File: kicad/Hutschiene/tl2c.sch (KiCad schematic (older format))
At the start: 29 parts, among them IC101 ATTINY20-X, P101 12VDC, P102 RJ45, P103 CTL CONN, P104 TPI Header, P105 DRV CONN, P106 240VAC, P108 UG, P109 5VDC, P110 EG, P111 OG, SW101 TL3315NF160Q

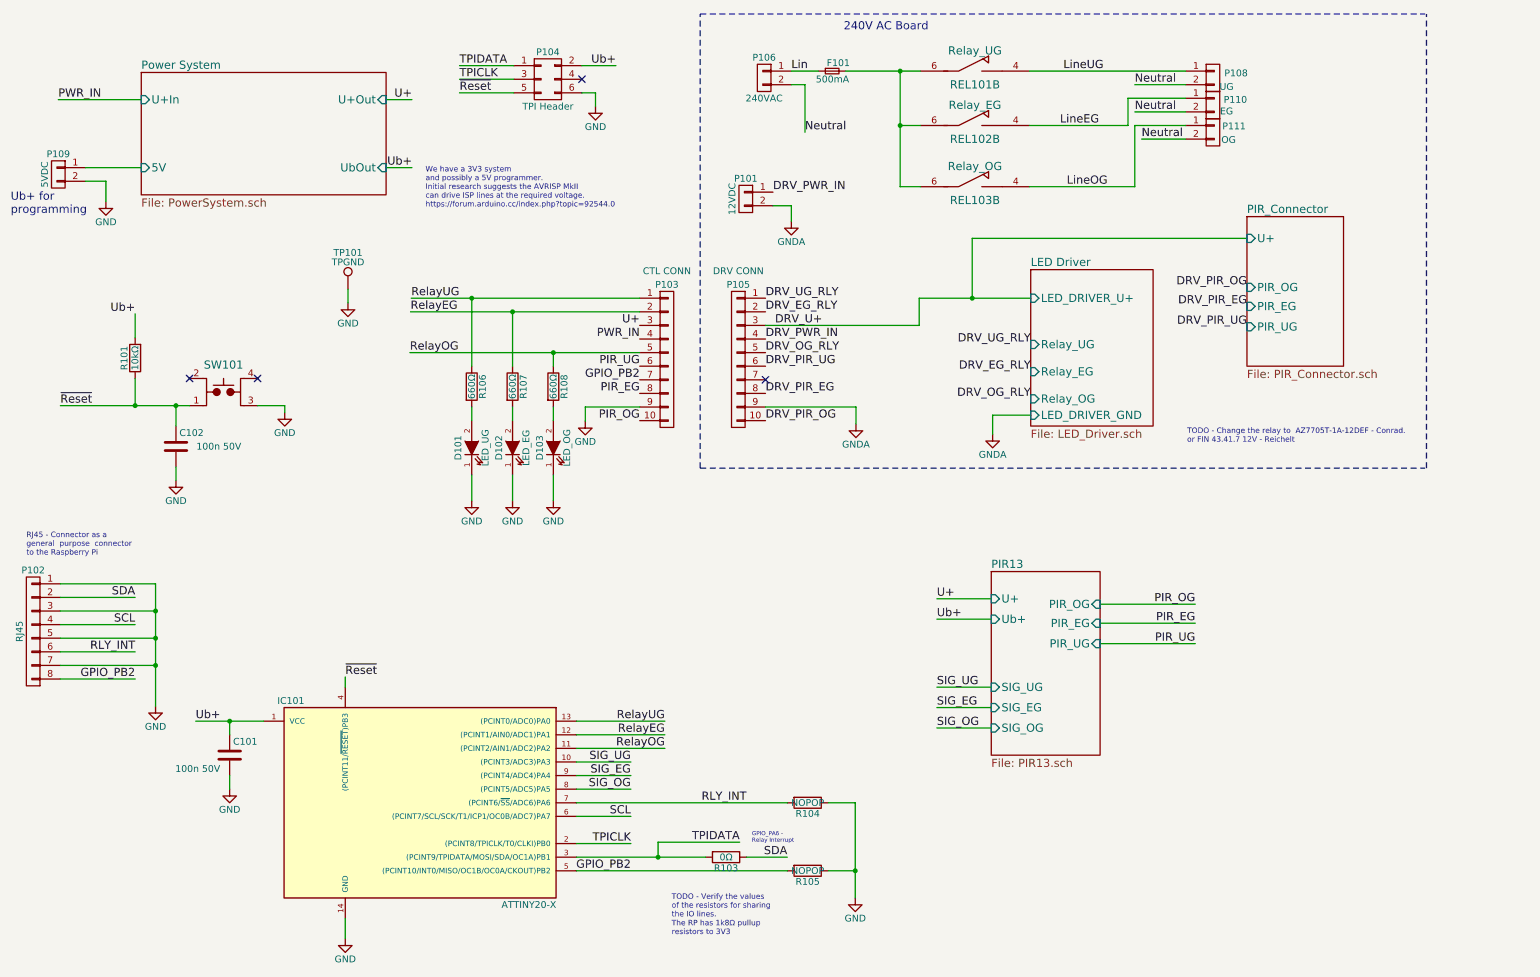
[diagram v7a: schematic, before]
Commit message: Correction to the board connected and seperated out the pwr
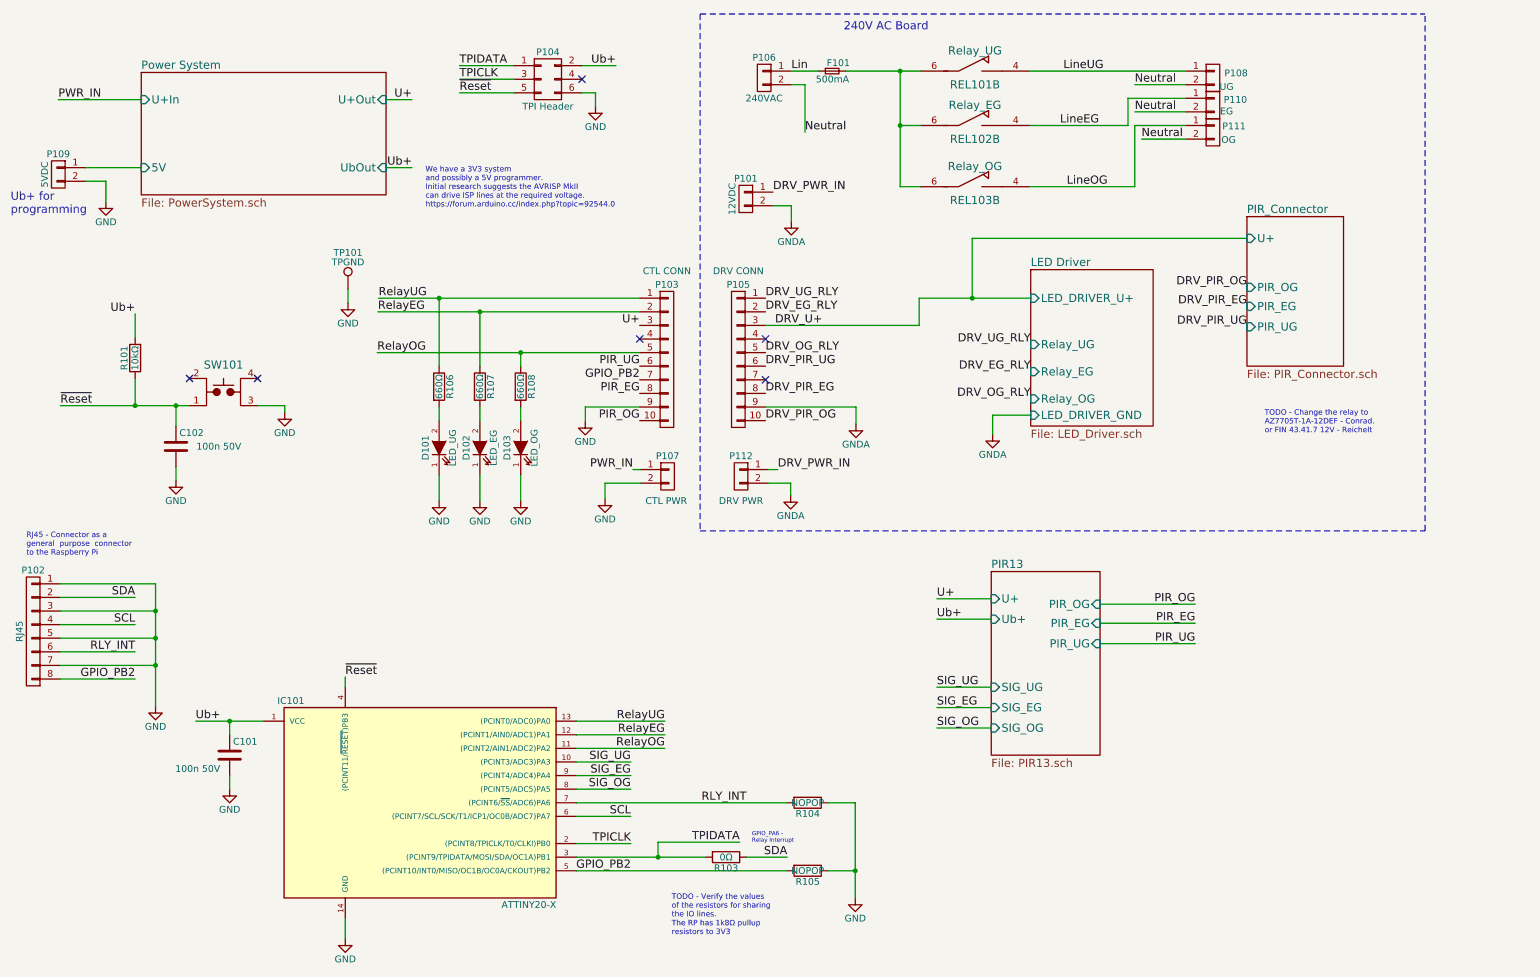
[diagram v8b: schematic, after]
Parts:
- added P107: CTL PWR, Pin_Headers:Pin_Header_Straight_1x02_Pitch2.54mm, symbol CONN_01X02
- added P112: DRV PWR, Pin_Headers:Pin_Header_Straight_1x02_Pitch2.54mm, symbol CONN_01X02
- P104: footprint tl2c-footprint:TC2030-IDC-FP_ISP_Connector -> Connect:Tag-Connect_TC2030-IDC-NL
- SW101: footprint tl2c-footprint:PTS525SM15SMTR2LFS -> tl2c-footprint:TACTILE_FSM2JSMAA
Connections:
- net DRV_PWR_IN: now also P112.1 (P1); no longer P105.4 (P4)
- net GND: now also P107.2 (P2)
- net GNDA: now also P112.2 (P2)
- net PWR_IN: now also P107.1 (P1); no longer P103.4 (P4)
- no-connect marks 4 -> 6
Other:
- note added: "TODO - Change the relay to \nAZ7705T-1A-12DEF - Conrad.\nor FIN 43.41.7 12V - Reichelt"
- note removed: "TODO - Change the relay to AZ7705T-1A-12DEF - Conrad.\nor FIN 43.41.7 12V - Reichelt"
- moved on the sheet: D101, D102, D103, R106, R107, R108
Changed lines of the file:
@@
 F6 "LED_DRIVER_GND" I L 8050 3670 60
 $EndSheet
-Text Label 3495 2810 0    60   ~ 0
+Text Label 3255 2810 0    60   ~ 0
 RelayUG
-Text Label 3490 2910 0    60   ~ 0
+Text Label 3250 2910 0    60   ~ 0
 RelayEG
-Text Label 3485 3210 0    60   ~ 0
+Text Label 3245 3210 0    60   ~ 0
 RelayOG
 $Comp
@@
 F 0 "SW101" V 2315 3500 60  0000 C CNN
 F 1 "TL3315NF160Q" H 2565 3550 60  0001 C CNN
-F 2 "tl2c-footprint:PTS525SM15SMTR2LFS" H 2115 3450 60  0001 C CNN
+F 2 "tl2c-footprint:TACTILE_FSM2JSMAA" H 2115 3450 60  0001 C CNN
 F 3 "" H 2115 3450 60  0000 C CNN
 F 4 "Value" H 2115 3500 60  0001 C CNN "MFP"
@@
 L LED D101
 U 1 1 5856AA32
-P 3940 3910
-F 0 "D101" H 3940 4010 50  0000 C CNN
-F 1 "LED_UG" H 3940 3810 50  0000 C CNN
-F 2 "LEDs:LED_0805" H 3940 3910 50  0001 C CNN
-F 3 "" H 3940 3910 50  0000 C CNN
-	1    3940 3910
+P 3700 3910
+F 0 "D101" H 3700 4010 50  0000 C CNN
+F 1 "LED_UG" H 3700 3810 50  0000 C CNN
+F 2 "LEDs:LED_0805" H 3700 3910 50  0001 C CNN
+F 3 "" H 3700 3910 50  0000 C CNN
+	1    3700 3910
 	0    -1   -1   0
 $EndComp
@@
 L R R106
 U 1 1 5856AB2B
-P 3940 3460
-F 0 "R106" V 4020 3460 50  0000 C CNN
-F 1 "660Ω" V 3940 3460 50  0000 C CNN
-F 2 "Resistors_SMD:R_0805" V 3870 3460 50  0001 C CNN
-F 3 "" H 3940 3460 50  0000 C CNN
-	1    3940 3460
+P 3700 3460
+F 0 "R106" V 3780 3460 50  0000 C CNN
+F 1 "660Ω" V 3700 3460 50  0000 C CNN
+F 2 "Resistors_SMD:R_0805" V 3630 3460 50  0001 C CNN
+F 3 "" H 3700 3460 50  0000 C CNN
+	1    3700 3460
 	1    0    0    -1
 $EndComp
@@
 L GND #PWR07
 U 1 1 5856AF1B
-P 3940 4300
-F 0 "#PWR07" H 3940 4050 50  0001 C CNN
-F 1 "GND" H 3940 4150 50  0000 C CNN
-F 2 "" H 3940 4300 50  0000 C CNN
-F 3 "" H 3940 4300 50  0000 C CNN
-	1    3940 4300
+P 3700 4300
+F 0 "#PWR07" H 3700 4050 50  0001 C CNN
+F 1 "GND" H 3700 4150 50  0000 C CNN
+F 2 "" H 3700 4300 50  0000 C CNN
+F 3 "" H 3700 4300 50  0000 C CNN
+	1    3700 4300
 	1    0    0    -1
 $EndComp
@@
 L LED D102
 U 1 1 5856B277
-P 4240 3910
-F 0 "D102" H 4240 4010 50  0000 C CNN
-F 1 "LED_EG" H 4240 3810 50  0000 C CNN
-F 2 "LEDs:LED_0805" H 4240 3910 50  0001 C CNN
-F 3 "" H 4240 3910 50  0000 C CNN
-	1    4240 3910
+P 4000 3910
+F 0 "D102" H 4000 4010 50  0000 C CNN
+F 1 "LED_EG" H 4000 3810 50  0000 C CNN
+F 2 "LEDs:LED_0805" H 4000 3910 50  0001 C CNN
+F 3 "" H 4000 3910 50  0000 C CNN
+	1    4000 3910
 	0    -1   -1   0
 $EndComp
@@
 L R R107
 U 1 1 5856B27D
-P 4240 3460
-F 0 "R107" V 4320 3460 50  0000 C CNN
-F 1 "660Ω" V 4240 3460 50  0000 C CNN
-F 2 "Resistors_SMD:R_0805" V 4170 3460 50  0001 C CNN
-F 3 "" H 4240 3460 50  0000 C CNN
-	1    4240 3460
+P 4000 3460
+F 0 "R107" V 4080 3460 50  0000 C CNN
+F 1 "660Ω" V 4000 3460 50  0000 C CNN
+F 2 "Resistors_SMD:R_0805" V 3930 3460 50  0001 C CNN
+F 3 "" H 4000 3460 50  0000 C CNN
+	1    4000 3460
 	1    0    0    -1
 $EndComp
@@
 L GND #PWR08
 U 1 1 5856B284
-P 4240 4300
-F 0 "#PWR08" H 4240 4050 50  0001 C CNN
-F 1 "GND" H 4240 4150 50  0000 C CNN
-F 2 "" H 4240 4300 50  0000 C CNN
-F 3 "" H 4240 4300 50  0000 C CNN
-	1    4240 4300
+P 4000 4300
+F 0 "#PWR08" H 4000 4050 50  0001 C CNN
+F 1 "GND" H 4000 4150 50  0000 C CNN
+F 2 "" H 4000 4300 50  0000 C CNN
+F 3 "" H 4000 4300 50  0000 C CNN
+	1    4000 4300
 	1    0    0    -1
 $EndComp
@@
 L LED D103
 U 1 1 5856B503
-P 4540 3910
-F 0 "D103" H 4540 4010 50  0000 C CNN
-F 1 "LED_OG" H 4540 3810 50  0000 C CNN
-F 2 "LEDs:LED_0805" H 4540 3910 50  0001 C CNN
-F 3 "" H 4540 3910 50  0000 C CNN
-	1    4540 3910
+P 4300 3910
+F 0 "D103" H 4300 4010 50  0000 C CNN
+F 1 "LED_OG" H 4300 3810 50  0000 C CNN
+F 2 "LEDs:LED_0805" H 4300 3910 50  0001 C CNN
+F 3 "" H 4300 3910 50  0000 C CNN
+	1    4300 3910
 	0    -1   -1   0
 $EndComp
@@
 L R R108
 U 1 1 5856B509
-P 4540 3460
-F 0 "R108" V 4620 3460 50  0000 C CNN
-F 1 "660Ω" V 4540 3460 50  0000 C CNN
-F 2 "Resistors_SMD:R_0805" V 4470 3460 50  0001 C CNN
-F 3 "" H 4540 3460 50  0000 C CNN
-	1    4540 3460
+P 4300 3460
+F 0 "R108" V 4380 3460 50  0000 C CNN
+F 1 "660Ω" V 4300 3460 50  0000 C CNN
+F 2 "Resistors_SMD:R_0805" V 4230 3460 50  0001 C CNN
+F 3 "" H 4300 3460 50  0000 C CNN
+	1    4300 3460
 	1    0    0    -1
 $EndComp
@@
 L GND #PWR09
 U 1 1 5856B510
-P 4540 4300
-F 0 "#PWR09" H 4540 4050 50  0001 C CNN
-F 1 "GND" H 4540 4150 50  0000 C CNN
-F 2 "" H 4540 4300 50  0000 C CNN
-F 3 "" H 4540 4300 50  0000 C CNN
-	1    4540 4300
+P 4300 4300
+F 0 "#PWR09" H 4300 4050 50  0001 C CNN
+F 1 "GND" H 4300 4150 50  0000 C CNN
+F 2 "" H 4300 4300 50  0000 C CNN
+F 3 "" H 4300 4300 50  0000 C CNN
+	1    4300 4300
 	1    0    0    -1
 $EndComp
@@
 	-1   0    0    -1
 $EndComp
-Text Notes 9200 3880 0    40   ~ 0
-TODO - Change the relay to  AZ7705T-1A-12DEF - Conrad.\nor FIN 43.41.7 12V - Reichelt
+Text Notes 9770 3810 0    40   ~ 0
+TODO - Change the relay to  \nAZ7705T-1A-12DEF - Conrad.\nor FIN 43.41.7 12V - Reichelt
 Text Label 5175 3010 2    60   ~ 0
 U+
@@
 F 0 "P104" H 4500 1400 50  0000 C CNN
 F 1 "TPI Header" H 4500 1000 50  0000 C CNN
-F 2 "tl2c-footprint:TC2030-IDC-FP_ISP_Connector" H 4500 0   50  0001 C CNN
+F 2 "Connect:Tag-Connect_TC2030-IDC-NL" H 4500 0   50  0001 C CNN
 F 3 "" H 4500 0   50  0000 C CNN
 F 4 "Value" H 4500 1200 60  0001 C CNN "MFP"
@@
 	-1   0    0    -1
 $EndComp
-Text Label 6100 3110 0    60   ~ 0
-DRV_PWR_IN
 NoConn ~ 6100 3410
 $Comp
@@
 Text Label 6170 3010 0    60   ~ 0
 DRV_U+
-Text Label 5175 3110 2    60   ~ 0
+Text Label 5125 4070 2    60   ~ 0
 PWR_IN
 Text Label 900  1350 0    60   ~ 0
@@
 Text Label 6155 2030 0    60   ~ 0
 DRV_PWR_IN
+$Comp
+L CONN_01X02 P107
+U 1 1 59A79123
+P 5380 4120
+F 0 "P107" H 5380 4270 50  0000 C CNN
+F 1 "CTL PWR" H 5370 3940 50  0000 C CNN
+F 2 "Pin_Headers:Pin_Header_Straight_1x02_Pitch2.54mm" H 5380 4120 60  0001 C CNN
+F 3 "" H 5380 4120 60  0000 C CNN
+	1    5380 4120
+	1    0    0    -1
+$EndComp
+$Comp
+L CONN_01X02 P112
+U 1 1 59A792BA
+P 5920 4120
+F 0 "P112" H 5920 4270 50  0000 C CNN
+F 1 "DRV PWR" H 5920 3940 50  0000 C CNN
+F 2 "Pin_Headers:Pin_Header_Straight_1x02_Pitch2.54mm" H 5920 4120 60  0001 C CNN
+F 3 "" H 5920 4120 60  0000 C CNN
+	1    5920 4120
+	-1   0    0    -1
+$EndComp
+Text Label 6190 4070 0    60   ~ 0
+DRV_PWR_IN
 Wire Wire Line
 	1910 5920 2410 5920
@@
 Connection ~ 1465 3600
 Wire Wire Line
-	3940 3610 3940 3710
-Wire Wire Line
-	4240 3610 4240 3710
-Wire Wire Line
-	4540 3610 4540 3710
+	3700 3610 3700 3710
+Wire Wire Line
+	4000 3610 4000 3710
+Wire Wire Line
+	4300 3610 4300 3710
 Wire Wire Line
 	6290 1140 6490 1140
@@
 Wire Notes Line
 	5620 720  10950 720
-Wire Notes Line
-	5620 4060 10950 4060
 Wire Wire Line
 	9640 2370 7620 2370
 Wire Wire Line
 	7620 2370 7620 2810
-Wire Notes Line
-	10960 4060 10960 720
-Wire Wire Line
-	3940 4110 3940 4300
-Wire Wire Line
-	4240 4110 4240 4300
-Wire Wire Line
-	4540 4110 4540 4300
+Wire Wire Line
+	3700 4110 3700 4300
+Wire Wire Line
+	4000 4110 4000 4300
+Wire Wire Line
+	4300 4110 4300 4300
 Wire Wire Line
 	7770 3810 7770 3670
 Wire Wire Line
 	7770 3670 8050 3670
-Wire Notes Line
-	5620 4060 5620 720
 Wire Wire Line
 	4775 3715 4775 3610
@@
 	6765 3610 6100 3610
 Wire Wire Line
-	3490 2910 5175 2910
-Wire Wire Line
-	3495 2810 5175 2810
+	3250 2910 5175 2910
+Wire Wire Line
+	3255 2810 5175 2810
 Wire Wire Line
 	7230 2810 7230 3010
@@
 	6290 2130 6290 2245
 Wire Wire Line
-	5175 3210 3485 3210
-Wire Wire Line
-	4540 3310 4540 3210
-Connection ~ 4540 3210
-Wire Wire Line
-	4240 3310 4240 2910
-Connection ~ 4240 2910
-Wire Wire Line
-	3940 3310 3940 2810
-Connection ~ 3940 2810
+	3245 3210 5175 3210
+Wire Wire Line
+	4300 3310 4300 3210
+Connection ~ 4300 3210
+Wire Wire Line
+	4000 3310 4000 2910
+Connection ~ 4000 2910
+Wire Wire Line
+	3700 3310 3700 2810
+Connection ~ 3700 2810
+Wire Notes Line
+	5620 720  5620 4520
+Wire Notes Line
+	5620 4520 10950 4520
+Wire Notes Line
+	10950 4520 10950 720
+Wire Wire Line
+	5180 4070 5125 4070
+Wire Wire Line
+	4920 4170 5180 4170
+Wire Wire Line
+	6120 4070 6190 4070
+$Comp
+L GNDA #PWR017
+U 1 1 59A89BF1
+P 6285 4260
+F 0 "#PWR017" H 6285 4010 50  0001 C CNN
+F 1 "GNDA" H 6285 4110 50  0000 C CNN
+F 2 "" H 6285 4260 60  0000 C CNN
+F 3 "" H 6285 4260 60  0000 C CNN
+	1    6285 4260
+	1    0    0    -1
+$EndComp
+Wire Wire Line
+	6285 4260 6285 4170
+Wire Wire Line
+	6285 4170 6120 4170
+$Comp
+L GND #PWR018
+U 1 1 59A8A3F7
+P 4920 4285
+F 0 "#PWR018" H 4920 4035 50  0001 C CNN
+F 1 "GND" H 4920 4135 50  0000 C CNN
+F 2 "" H 4920 4285 50  0000 C CNN
+F 3 "" H 4920 4285 50  0000 C CNN
+	1    4920 4285
+	1    0    0    -1
+$EndComp
+Wire Wire Line
+	4920 4170 4920 4285
+NoConn ~ 6100 3110
+NoConn ~ 5175 3110
 $EndSCHEMATC
